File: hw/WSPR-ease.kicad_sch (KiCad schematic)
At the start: 51 parts, among them J101 SMA, J102 pwr+data, J103 SMA, Q101 2N7002H, U101 GNSS module, U102 ESP32-S3-WROOM-1-N8R8, U103 SRV05-4, U104 TPS74612PQWDRBRQ1, U105 TPS22918DBVR, U106 LMR51430YDDCR

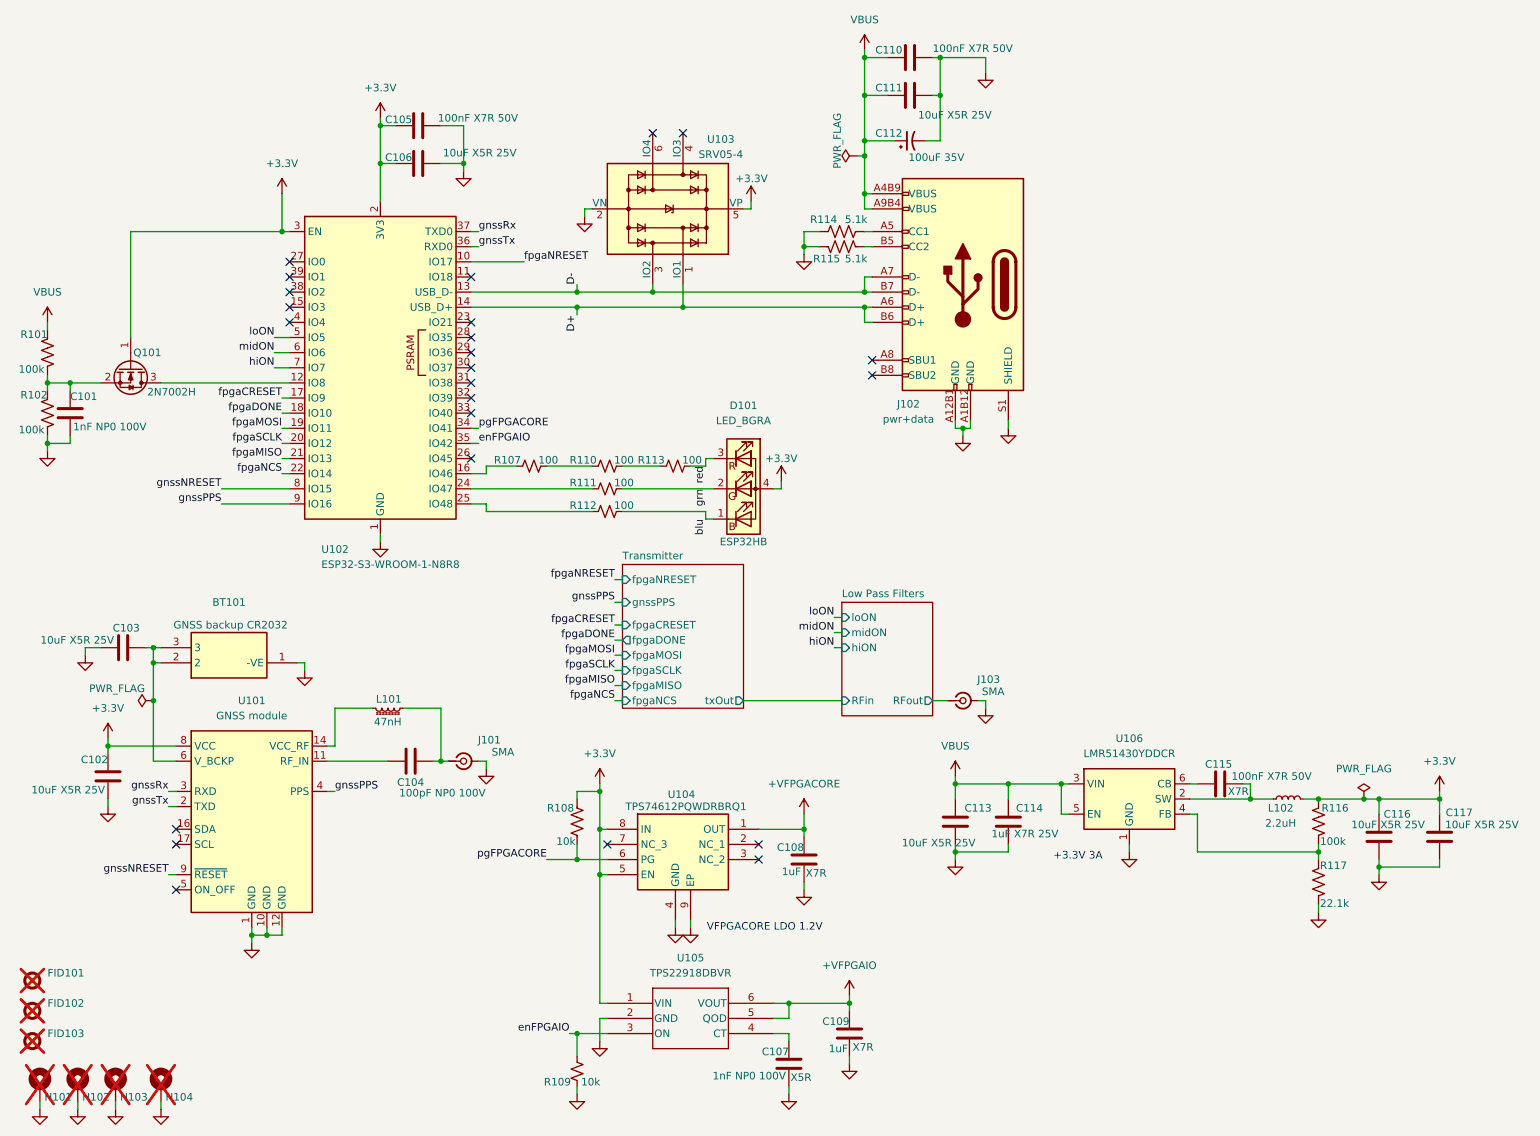
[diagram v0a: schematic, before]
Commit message: Use VFPGAIO for pullup for driverNEN. Fix some layout issues with more equal routing lengths in critical tx phase paths.
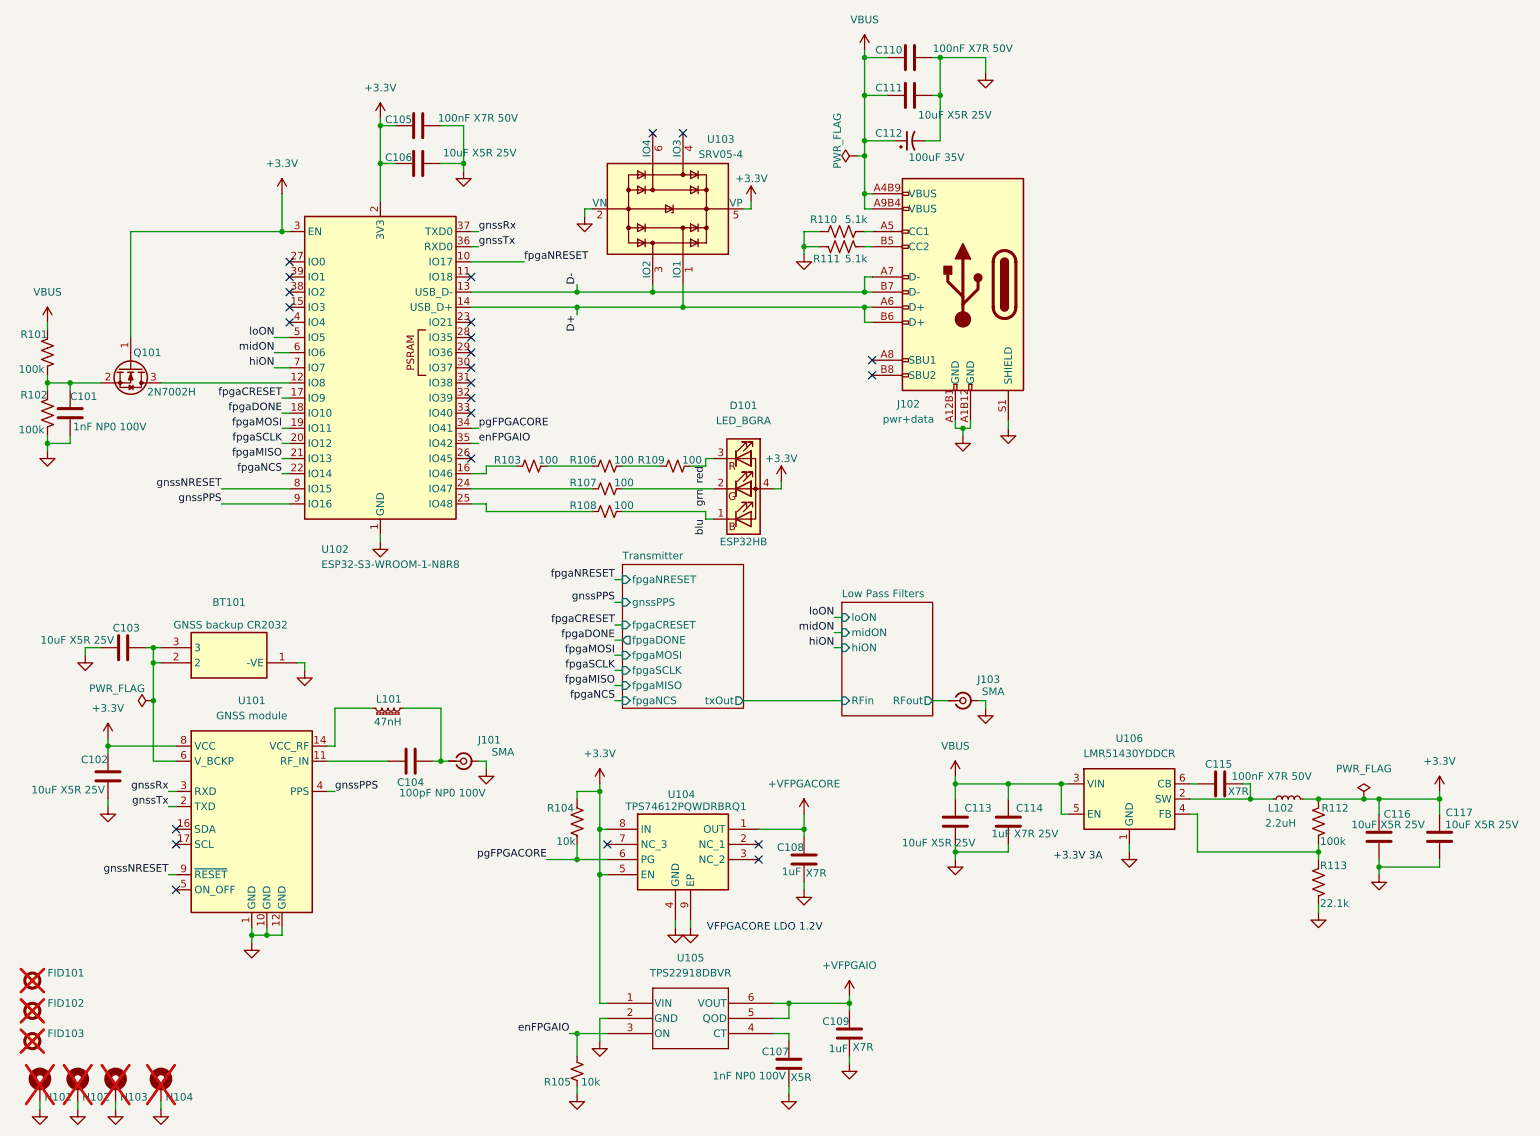
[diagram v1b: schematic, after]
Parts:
- renumbered R107 to R103, R108 to R104, R109 to R105, R110 to R106, R111 to R107, R112 to R108, R113 to R109, R114 to R110, R115 to R111, R116 to R112, R117 to R113
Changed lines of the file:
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@@
 		(on_board yes)
 		(dnp no)
-		(property "Reference" "R108"
+		(property "Reference" "R104"
 			(at 106.172 150.114 0)
 			(effects
@@
 			(project "WSPR-ease"
 				(path "/31075357-d7d2-474d-bd47-511c83e129b3"
-					(reference "R108")
+					(reference "R104")
 					(unit 1)
 				)
@@
 		(on_board yes)
 		(dnp no)
-		(property "Reference" "R112"
+		(property "Reference" "R108"
 			(at 107.696 99.314 90)
 			(effects
@@
 			(project "WSPR-ease"
 				(path "/31075357-d7d2-474d-bd47-511c83e129b3"
-					(reference "R112")
+					(reference "R108")
 					(unit 1)
 				)
@@
 		(on_board yes)
 		(dnp no)
-		(property "Reference" "R107"
+		(property "Reference" "R103"
 			(at 94.996 91.694 90)
 			(effects
@@
 			(project "WSPR-ease"
 				(path "/31075357-d7d2-474d-bd47-511c83e129b3"
-					(reference "R107")
+					(reference "R103")
 					(unit 1)
 				)
@@
 		(on_board yes)
 		(dnp no)
-		(property "Reference" "R109"
+		(property "Reference" "R105"
 			(at 103.378 196.088 0)
 			(effects
@@
 			(project "WSPR-ease"
 				(path "/31075357-d7d2-474d-bd47-511c83e129b3"
-					(reference "R109")
+					(reference "R105")
 					(unit 1)
 				)
@@
 		(on_board yes)
 		(dnp no)
-		(property "Reference" "R114"
+		(property "Reference" "R110"
 			(at 145.796 51.308 90)
 			(effects
@@
 			(project "WSPR-ease"
 				(path "/31075357-d7d2-474d-bd47-511c83e129b3"
-					(reference "R114")
+					(reference "R110")
 					(unit 1)
 				)
@@
 		(on_board yes)
 		(dnp no)
-		(property "Reference" "R110"
+		(property "Reference" "R106"
 			(at 107.696 91.694 90)
 			(effects
@@
 			(project "WSPR-ease"
 				(path "/31075357-d7d2-474d-bd47-511c83e129b3"
-					(reference "R110")
+					(reference "R106")
 					(unit 1)
 				)
@@
 		(on_board yes)
 		(dnp no)
-		(property "Reference" "R111"
+		(property "Reference" "R107"
 			(at 107.696 95.504 90)
 			(effects
@@
 			(project "WSPR-ease"
 				(path "/31075357-d7d2-474d-bd47-511c83e129b3"
-					(reference "R111")
+					(reference "R107")
 					(unit 1)
 				)
@@
 		(on_board yes)
 		(dnp no)
-		(property "Reference" "R113"
+		(property "Reference" "R109"
 			(at 119.126 91.694 90)
 			(effects
@@
 			(project "WSPR-ease"
 				(path "/31075357-d7d2-474d-bd47-511c83e129b3"
-					(reference "R113")
+					(reference "R109")
 					(unit 1)
 				)
@@
 		(on_board yes)
 		(dnp no)
-		(property "Reference" "R117"
+		(property "Reference" "R113"
 			(at 231.394 159.766 0)
 			(effects
@@
 			(project "WSPR-ease"
 				(path "/31075357-d7d2-474d-bd47-511c83e129b3"
-					(reference "R117")
+					(reference "R113")
 					(unit 1)
 				)
@@
 		(on_board yes)
 		(dnp no)
-		(property "Reference" "R116"
+		(property "Reference" "R112"
 			(at 231.648 150.114 0)
 			(effects
@@
 			(project "WSPR-ease"
 				(path "/31075357-d7d2-474d-bd47-511c83e129b3"
-					(reference "R116")
+					(reference "R112")
 					(unit 1)
 				)
@@
 		(on_board yes)
 		(dnp no)
-		(property "Reference" "R115"
+		(property "Reference" "R111"
 			(at 146.304 57.912 90)
 			(effects
@@
 			(project "WSPR-ease"
 				(path "/31075357-d7d2-474d-bd47-511c83e129b3"
-					(reference "R115")
+					(reference "R111")
 					(unit 1)
 				)

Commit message: Fucking USB 16-pin footprint! Also, completely redid the layout and wiring of the transmitter using a MOSFET gate and R+diode gate drive, simplify BOM, enhance LPFs for square wave output >= 10MHz.
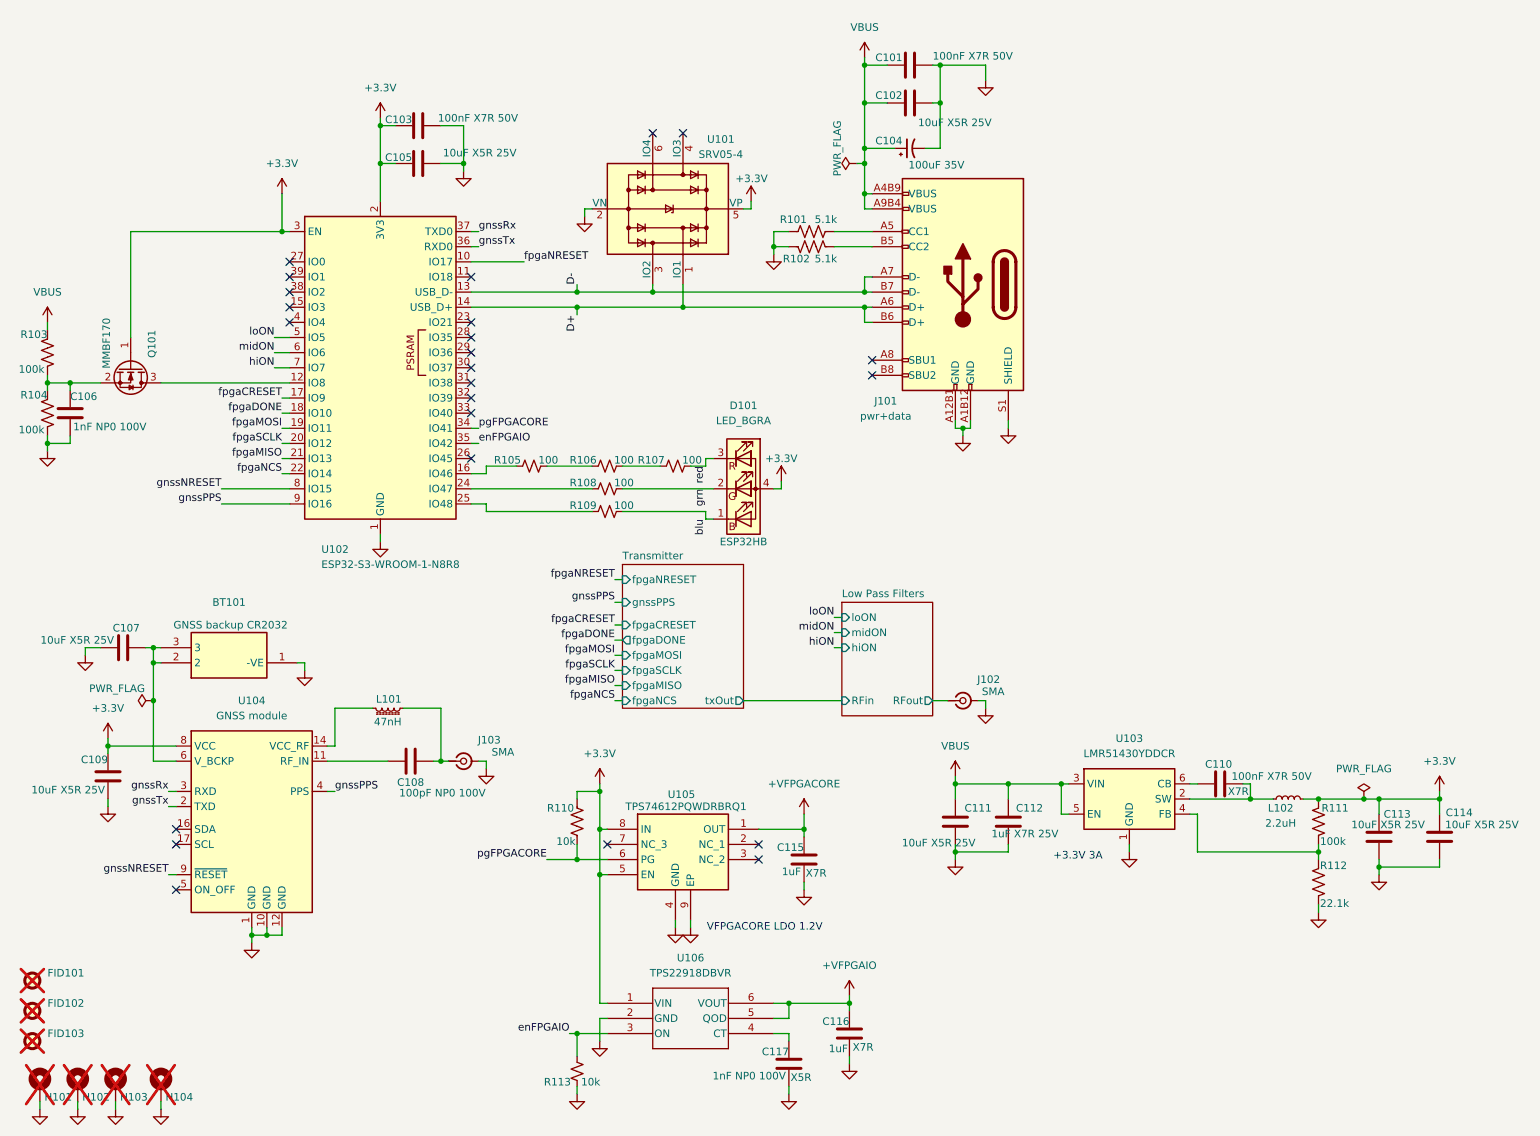
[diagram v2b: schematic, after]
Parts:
- removed Q101: 2N7002H, Package_TO_SOT_SMD:SOT-23, symbol Transistor_FET:2N7002H
- added Q101: MMBF170, Package_TO_SOT_SMD:SOT-23, symbol Transistor_FET:BS170F
- C101: renamed from C110; cap-type (none) -> X7R; working-voltage (none) -> 50V
- C102: renamed from C111; working-voltage (none) -> 25V
- C103: renamed from C105; cap-type (none) -> X7R; working-voltage (none) -> 50V
- C105: renamed from C106; working-voltage (none) -> 25V
- C106: renamed from C101; cap-type (none) -> X5R; working-voltage (none) -> 25V
- C107: renamed from C103; working-voltage (none) -> 25V
- C109: renamed from C102; working-voltage (none) -> 25V
- J101: renamed from J102; LCSC_PN C165948 -> (none); MPN TYPE-C-31-M-12 -> UJ20-C-H-G-SMT-2A-P16-TR; Manufacturer Korean HROparts Elec -> Same Sky; Mouser_PN (none) -> 179-CHGSMT2AP16TR
- R105: renamed from R103; MFG (none) -> Bourns; MPN (none) -> CR0402-JW-101GLF; Mouser_PN (none) -> 652-CR0402JW-101GLF
- R106: MFG (none) -> Bourns; MPN (none) -> CR0402-JW-101GLF; Mouser_PN (none) -> 652-CR0402JW-101GLF
- R107: renamed from R109; MFG (none) -> Bourns; MPN (none) -> CR0402-JW-101GLF; Mouser_PN (none) -> 652-CR0402JW-101GLF
- R108: renamed from R107; MFG (none) -> Bourns; MPN (none) -> CR0402-JW-101GLF; Mouser_PN (none) -> 652-CR0402JW-101GLF
- R109: renamed from R108; MFG (none) -> Bourns; MPN (none) -> CR0402-JW-101GLF; Mouser_PN (none) -> 652-CR0402JW-101GLF
- R113: renamed from R105; MFG (none) -> Bourns; MPN (none) -> CRT0402-FZ-1003GLF; Mouser_PN (none) -> 652-CRT0402FZ1003GLF
- renumbered C112 to C104, C104 to C108, C115 to C110, C113 to C111, C114 to C112, C116 to C113, C117 to C114, C108 to C115, C109 to C116, C107 to C117, J103 to J102, J101 to J103, R110 to R101, R111 to R102, R101 to R103, R102 to R104, R104 to R110, R112 to R111, R113 to R112, U103 to U101, U106 to U103, U101 to U104, U104 to U105, U105 to U106
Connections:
- net +3.3V: now also Q101.1 (G)
- net at C106.1, R103.2, R104.1: now also Q101.2 (S)
- net at U102.12 (IO8): now also Q101.3 (D)
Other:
- moved on the sheet: C101, C102, C104, R101, R102

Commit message: Add symbols for new components, switch to SI5351 in place of FPGA. Simplify!
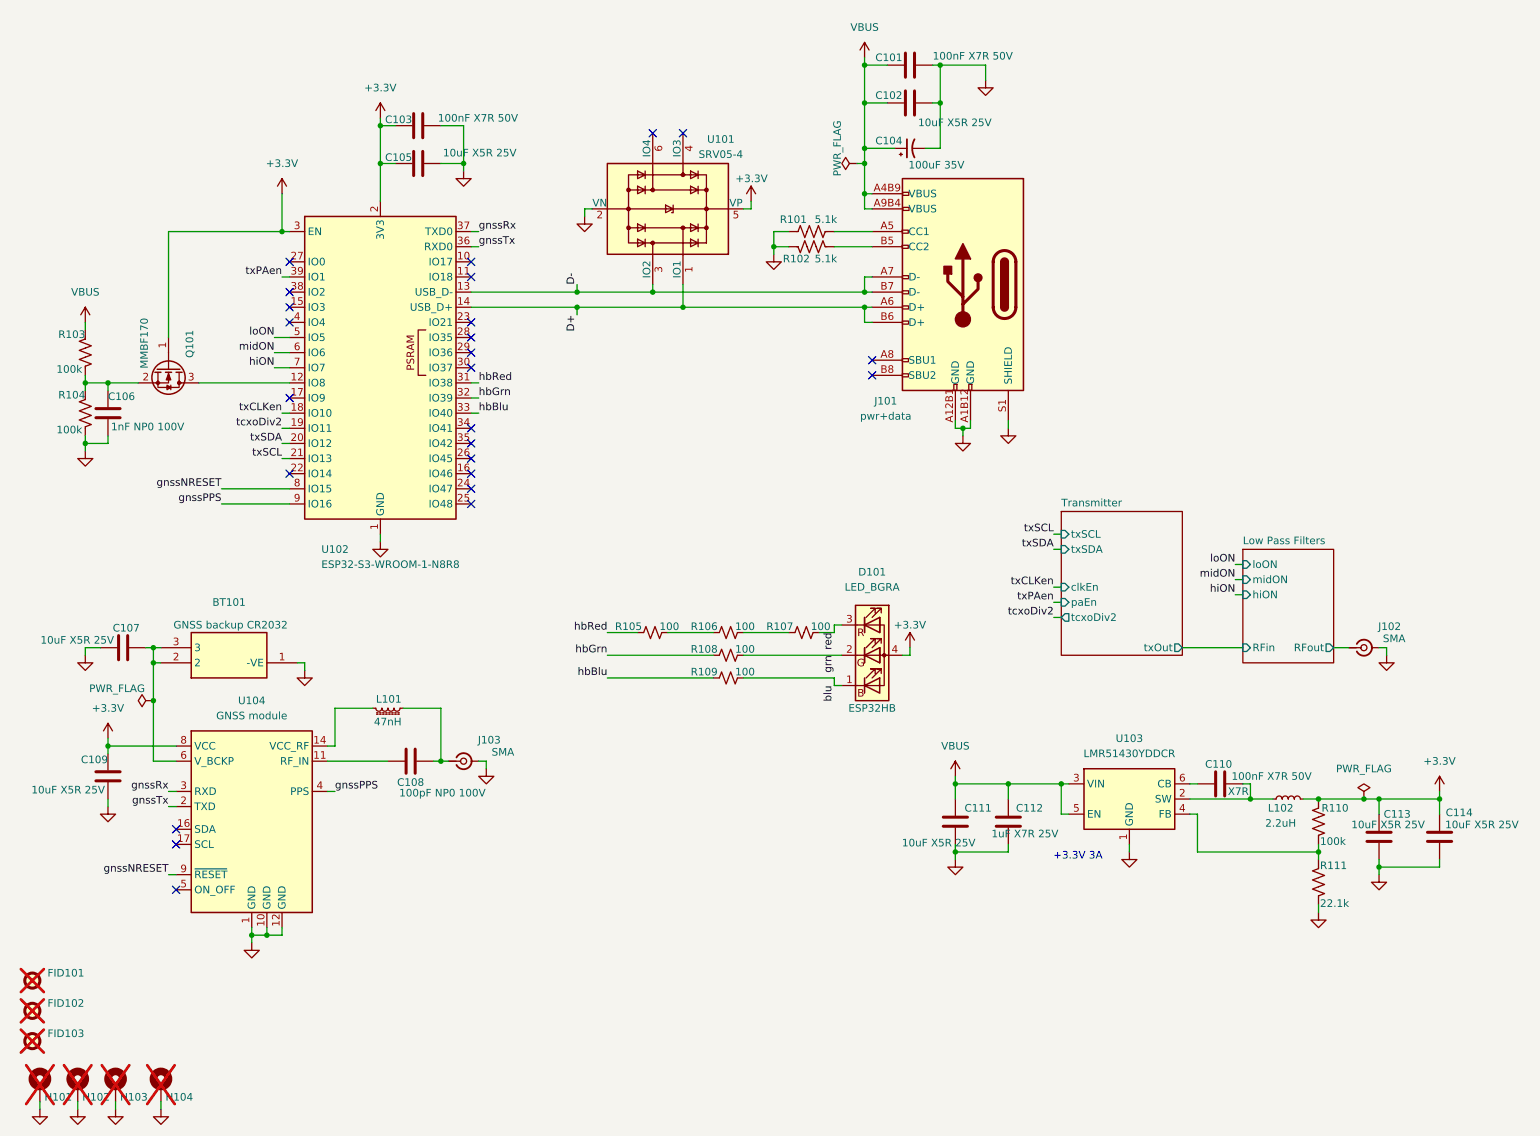
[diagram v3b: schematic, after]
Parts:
- removed C115, C116: 1uF, Capacitor_SMD:C_0402_1005Metric, symbol Device:C
- removed C117: 1nF NP0 100V, Capacitor_SMD:C_0603_1608Metric, symbol Device:C
- removed R110: 10k, Resistor_SMD:R_0402_1005Metric, symbol Device:R_US
- removed R113: 10k, Resistor_SMD:R_0402_1005Metric, symbol Device:R_Small_US
- removed U105: TPS74612PQWDRBRQ1, Library:SON65P300X300X100-9N-D, symbol Library:TPS74612PQWDRBRQ1
- removed U106: TPS22918DBVR, Library:DBV6_TEX, symbol Library:TPS22918DBVR
- renumbered R111 to R110, R112 to R111
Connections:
- net at U102.25 (IO48): no longer R109.1
- net at U102.16 (IO46): no longer R105.1
- net at U102.24 (IO47): no longer R108.1
- net hbRed: now reaches U102.31 (IO38)
- net hbRed: now also R105.1
- net hbGrn: now reaches U102.32 (IO39)
- net hbGrn: now also R108.1
- net hbBlu: now reaches U102.33 (IO40)
- net hbBlu: now also R109.1
- net txPAen: now reaches U102.39 (IO1)
- net enFPGAIO: no longer names the net of U102.35 (IO42)
- net fpgaCRESET: no longer names the net of U102.17 (IO9)
- net fpgaDONE renamed txCLKen
- net fpgaMISO renamed txSCL
- net fpgaMOSI renamed tcxoDiv2
- net fpgaNCS: no longer names the net of U102.22 (IO14)
- net fpgaNRESET: no longer names the net of U102.10 (IO17)
- net fpgaSCLK renamed txSDA
- net pgFPGACORE: no longer names the net of U102.34 (IO41)
- no-connect marks 24 -> 25
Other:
- sheet Transmitter ports: added clkEn, paEn, tcxoDiv2, txSCL, txSDA; removed fpgaCRESET, fpgaDONE, fpgaMISO, fpgaMOSI, fpgaNCS, fpgaNRESET, fpgaSCLK, gnssPPS
- note removed: "VFPGACORE LDO 1.2V"
- moved on the sheet: C106, D101, J102, Q101, R103, R104, R105, R106, R107, R108, R109
